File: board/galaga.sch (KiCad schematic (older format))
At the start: 13 parts, among them J1 led_a, J2 speaker_out, J3 led_b, J4 led_c, J5 pwr_in, U1 LD1117S33TR_SOT223, U2 ATmega328P-PU, U3 LM386, U4 BOB-00544

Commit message: added self-power-off hardware to schematic
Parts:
- added Q?: 2N7000, Package_TO_SOT_THT:TO-92_Inline, symbol Transistor_FET:2N7000
- added R?: 10M, symbol Device:R
- added R?: 20K, symbol Device:R
- added R?: 180R, symbol Device:R
- added SW?: SW_Push, symbol Switch:SW_Push
- added U?: LTV-817M, Package_DIP:DIP-4_W10.16mm, symbol Isolator:LTV-817M
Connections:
- net +9V: now also R?.1, SW?.1
- net GND: now also Q?.1 (S), U?.3; no longer J4.2 (Pin_2), J4.3 (Pin_3), R1.2, RV1.1, U1.1 (GND), U2.22 (GND), U2.8 (GND), U3.2 (-), U4.3 (GND)
- net at U2.2 (PD0): no longer J4.1 (Pin_1)
- net PWR_OFF: now reaches U2.9 (XTAL1/PB6)
- net PWR_OFF: now also R?.1
- new net: R1.2, RV1.1
- new net: R?.2, U?.1
- new net: Q?.2 (G), R?.2, U?.4
- new net: R?.1, SW?.2
- new net DGND: J4.1 (Pin_1), J4.2 (Pin_2), J4.3 (Pin_3), Q?.3 (D), R?.2, U1.1 (GND), U2.22 (GND), U2.8 (GND), U3.2 (-), U4.3 (GND), U?.2
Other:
- moved on the sheet: C1, C5, J1, J2, J3, J4, J5, U1, U2, U3, U4

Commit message: started laying out board - doesn't have to be perfect (cuz it's perfboard) and there's some vertical room I'm playing with
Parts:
- removed RV1: 1k, Potentiometer_THT:Potentiometer_Vishay_T7-YA_Single_Vertical, symbol Device:R_POT
- Q1: renamed from Q?; footprint Package_TO_SOT_THT:TO-92_Inline -> Package_TO_SOT_THT:TO-220-3_Vertical
- R2, R3, R4: renamed from R?; footprint (none) -> Resistor_THT:R_Axial_DIN0207_L6.3mm_D2.5mm_P2.54mm_Vertical
- SW1: renamed from SW?; footprint (none) -> TerminalBlock_TE-Connectivity:TerminalBlock_TE_282834-2_1x02_P2.54mm_Horizontal
- U4: footprint custom:bob-00544 -> Connector_PinHeader_2.54mm:PinHeader_1x07_P2.54mm_Vertical
- gave numbers to parts that had none: 1
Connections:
- net sd_cs: now also U2.16 (PB2); no longer U2.6 (PD4)
- net at C1.2: now also R1.2
- net sd_cd: no longer names the net of U2.5 (PD3)
- net sd_cd: no longer U4.1 (CD)
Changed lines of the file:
@@
 EESchema Schematic File Version 4
+LIBS:galaga-cache
 EELAYER 26 0
 EELAYER END
@@
 F 0 "U4" H 8381 3425 50  0000 C CNN
 F 1 "BOB-00544" H 8381 3334 50  0000 C CNN
-F 2 "custom:bob-00544" H 8300 3900 50  0001 C CNN
+F 2 "Connector_PinHeader_2.54mm:PinHeader_1x07_P2.54mm_Vertical" H 8300 3900 50  0001 C CNN
 F 3 "" H 8300 3900 50  0001 C CNN
 	1    8350 2900
@@
 Wire Wire Line
 	7750 2200 6050 2200
-Wire Wire Line
-	7550 3200 8100 3200
 Text GLabel 8050 3000 0    50   Input ~ 0
 DGND
@@
 Wire Wire Line
 	6050 3300 6400 3300
-Wire Wire Line
-	7550 3200 7550 3900
-Wire Wire Line
-	6050 3900 7550 3900
 Text HLabel 8050 2600 0    50   Input ~ 0
 sd_cs
 Wire Wire Line
 	8050 2600 8100 2600
-Text HLabel 6100 4000 2    50   Input ~ 0
+Text HLabel 6100 2100 2    50   Input ~ 0
 sd_cs
-Wire Wire Line
-	6050 4000 6100 4000
 Text Label 7200 2200 0    50   ~ 0
 sd_di
-Text Label 7550 3300 0    50   ~ 0
-sd_cd
 Text Label 7200 2400 0    50   ~ 0
 sd_sck
@@
 	1    0    0    -1
 $EndComp
-$Comp
-L Device:R_POT RV1
-U 1 1 5C58E151
-P 7000 2000
-F 0 "RV1" V 6886 2000 50  0001 C CNN
-F 1 "1k" V 7000 2000 50  0000 C CNN
-F 2 "Potentiometer_THT:Potentiometer_Vishay_T7-YA_Single_Vertical" H 7000 2000 50  0001 C CNN
-F 3 "~" H 7000 2000 50  0001 C CNN
-	1    7000 2000
-	0    -1   -1   0
-$EndComp
 Wire Wire Line
 	6050 2000 6100 2000
@@
 Wire Wire Line
 	8100 1400 8100 2000
-Wire Wire Line
-	8100 2000 7200 2000
-Wire Wire Line
-	7000 1850 7000 1800
-Wire Wire Line
-	7000 1800 7200 1800
-Wire Wire Line
-	7200 1800 7200 2000
-Wire Wire Line
-	7200 2000 7150 2000
 Text Notes 6200 1600 0    50   ~ 0
 With 3.3v max out of the m328, \nthis guarantees a maximum of \n2.62v into the amp. This would \nclip on full strength signals, but \nit allows us to take advantage of \nthe fact that audio is very rarely \nfull strength.
@@
 	8600 1500 8750 1500
 $Comp
-L Isolator:LTV-817M U?
+L Isolator:LTV-817M U5
 U 1 1 5D708174
 P 2450 2150
-F 0 "U?" H 2450 2475 50  0001 C CNN
+F 0 "U5" H 2450 2475 50  0001 C CNN
 F 1 "LTV-817M" H 2450 2384 50  0001 C CNN
 F 2 "Package_DIP:DIP-4_W10.16mm" H 2450 1850 50  0001 C CNN
@@
 $EndComp
 $Comp
-L Transistor_FET:2N7000 Q?
+L Transistor_FET:2N7000 Q1
 U 1 1 5D708462
 P 1450 1950
-F 0 "Q?" H 1655 1996 50  0001 L CNN
+F 0 "Q1" H 1655 1996 50  0001 L CNN
 F 1 "2N7000" H 1655 1905 50  0001 L CNN
-F 2 "Package_TO_SOT_THT:TO-92_Inline" H 1650 1875 50  0001 L CIN
+F 2 "Package_TO_SOT_THT:TO-220-3_Vertical" H 1650 1875 50  0001 L CIN
 F 3 "https://www.fairchildsemi.com/datasheets/2N/2N7000.pdf" H 1450 1950 50  0001 L CNN
 	1    1450 1950
@@
 $EndComp
 $Comp
-L Device:R R?
+L Device:R R2
 U 1 1 5D7084DD
 P 1350 1500
-F 0 "R?" H 1420 1546 50  0000 L CNN
+F 0 "R2" H 1420 1546 50  0000 L CNN
 F 1 "10M" H 1420 1455 50  0000 L CNN
-F 2 "" V 1280 1500 50  0001 C CNN
+F 2 "Resistor_THT:R_Axial_DIN0207_L6.3mm_D2.5mm_P2.54mm_Vertical" V 1280 1500 50  0001 C CNN
 F 3 "~" H 1350 1500 50  0001 C CNN
 	1    1350 1500
@@
 $EndComp
 $Comp
-L Device:R R?
+L Device:R R3
 U 1 1 5D70854B
 P 2750 1650
-F 0 "R?" H 2820 1696 50  0000 L CNN
+F 0 "R3" H 2820 1696 50  0000 L CNN
 F 1 "20K" H 2820 1605 50  0000 L CNN
-F 2 "" V 2680 1650 50  0001 C CNN
+F 2 "Resistor_THT:R_Axial_DIN0207_L6.3mm_D2.5mm_P2.54mm_Vertical" V 2680 1650 50  0001 C CNN
 F 3 "~" H 2750 1650 50  0001 C CNN
 	1    2750 1650
@@
 $EndComp
 $Comp
-L Switch:SW_Push SW?
+L Switch:SW_Push SW1
 U 1 1 5D7085A6
 P 2750 1100
-F 0 "SW?" V 2704 1248 50  0001 L CNN
+F 0 "SW1" V 2704 1248 50  0001 L CNN
 F 1 "SW_Push" V 2795 1248 50  0001 L CNN
-F 2 "" H 2750 1300 50  0001 C CNN
+F 2 "TerminalBlock_TE-Connectivity:TerminalBlock_TE_282834-2_1x02_P2.54mm_Horizontal" H 2750 1300 50  0001 C CNN
 F 3 "" H 2750 1300 50  0001 C CNN
 	1    2750 1100
 	0    1    1    0
 $EndComp
-Connection ~ 7200 2000
 Wire Wire Line
 	6050 2400 7650 2400
@@
 Wire Wire Line
 	8350 1250 8350 1600
-Wire Wire Line
-	6400 2000 6850 2000
 Text GLabel 6400 3400 0    50   Input ~ 0
 DGND
@@
 	1200 2250 1350 2250
 $Comp
-L Device:R R?
+L Device:R R4
 U 1 1 5D77529A
 P 2950 2050
-F 0 "R?" V 2743 2050 50  0000 C CNN
+F 0 "R4" V 2743 2050 50  0000 C CNN
 F 1 "180R" V 2834 2050 50  0000 C CNN
-F 2 "" V 2880 2050 50  0001 C CNN
+F 2 "Resistor_THT:R_Axial_DIN0207_L6.3mm_D2.5mm_P2.54mm_Vertical" V 2880 2050 50  0001 C CNN
 F 3 "~" H 2950 2050 50  0001 C CNN
 	1    2950 2050
@@
 Wire Wire Line
 	2750 1300 2750 1500
+Wire Wire Line
+	6400 2000 8100 2000
+Wire Wire Line
+	6100 2100 6050 2100
 $EndSCHEMATC

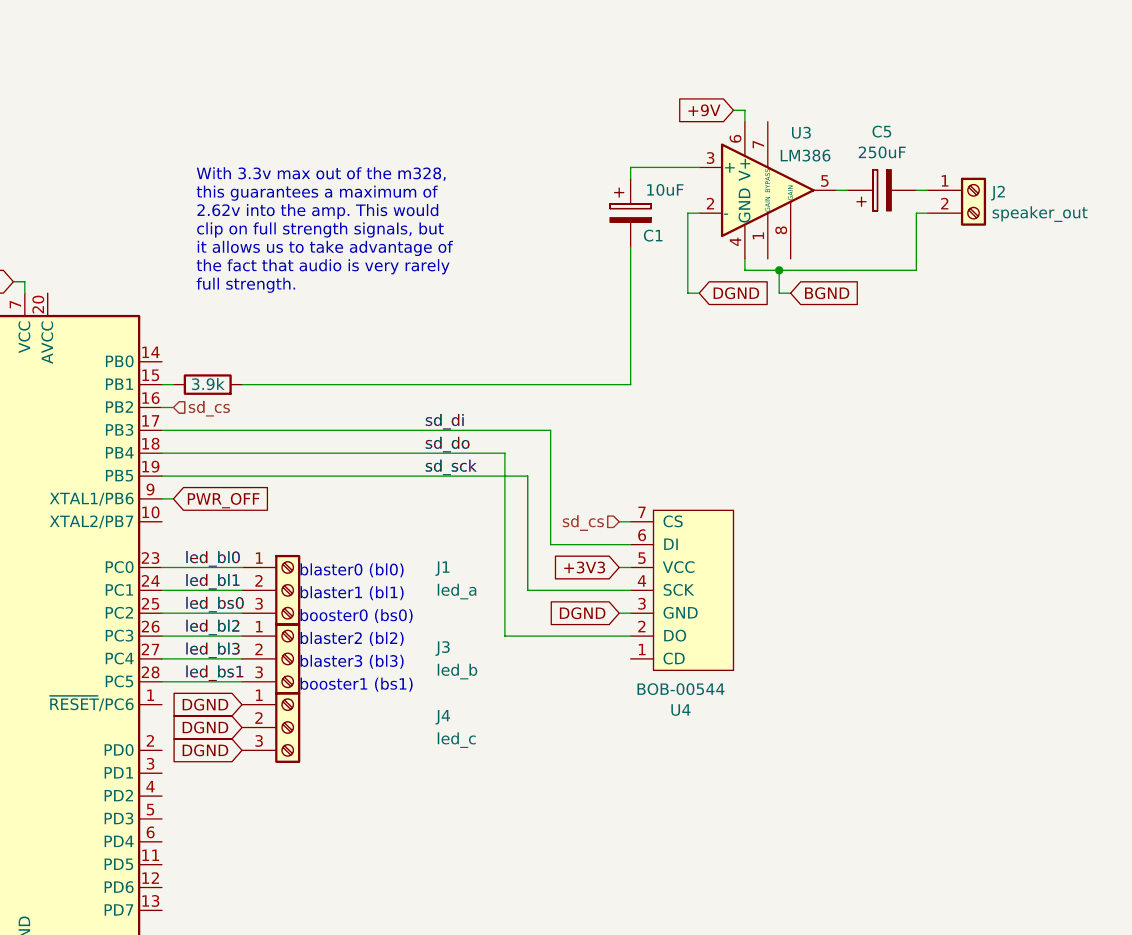
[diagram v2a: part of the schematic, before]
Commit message: changed SD CS pin to PORTB7 for better board layout
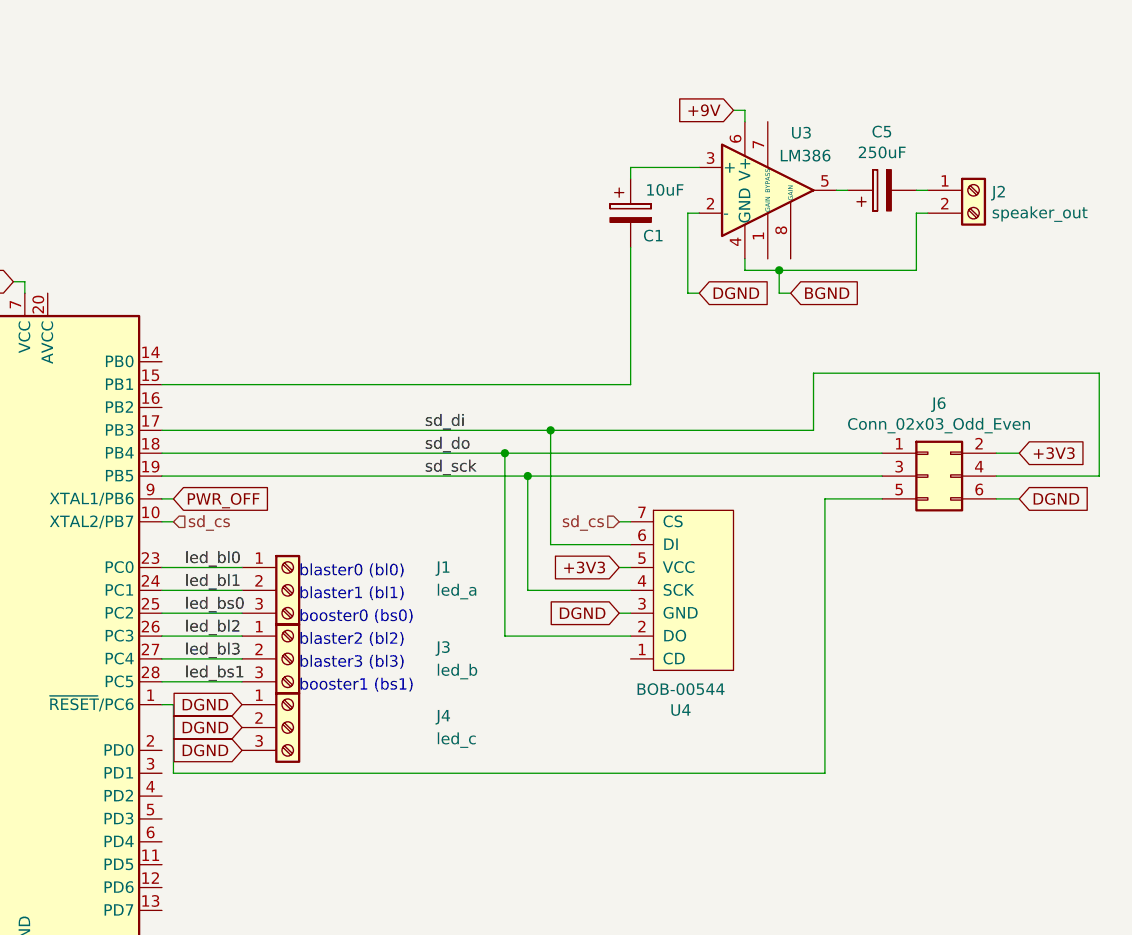
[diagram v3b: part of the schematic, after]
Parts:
- removed R1: 3.9k, Resistor_THT:R_Axial_DIN0207_L6.3mm_D2.5mm_P2.54mm_Vertical, symbol Device:R
- added J6: Conn_02x03_Odd_Even, Connector_PinHeader_2.54mm:PinHeader_2x03_P2.54mm_Vertical, symbol Connector_Generic:Conn_02x03_Odd_Even
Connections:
- net +3V3: now also J6.2 (Pin_2)
- net DGND: now also J6.6 (Pin_6)
- net sd_cs: now also U2.10 (XTAL2/PB7); no longer U2.16 (PB2)
- net sd_di: now also J6.4 (Pin_4)
- net sd_do: now also J6.1 (Pin_1)
- net sd_sck: now also J6.3 (Pin_3)
- net at U2.1 (~RESET~/PC6): now also J6.5 (Pin_5)
- net at U2.15 (PB1): now also C1.2
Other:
- note removed: "With 3.3v max out of the m328, \nthis guarantees a maximum of \n2.62v into the amp. This would \nclip on full strength signals, but \nit allows us to take advantage of \nthe fact that audio is very rarely \nfull strength."
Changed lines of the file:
@@
-$EndComp
-$Comp
-L Device:R R1
-U 1 1 5BBECF45
-P 6250 2000
-F 0 "R1" V 6600 2000 50  0001 R CNN
-F 1 "3.9k" V 6250 2000 50  0000 C CNN
-F 2 "Resistor_THT:R_Axial_DIN0207_L6.3mm_D2.5mm_P2.54mm_Vertical" V 6180 2000 50  0001 C CNN
-F 3 "~" H 6250 2000 50  0001 C CNN
-	1    6250 2000
-	0    -1   -1   0
 $EndComp
 $Comp
@@
 Wire Wire Line
 	8050 2600 8100 2600
-Text HLabel 6100 2100 2    50   Input ~ 0
+Text HLabel 6100 2600 2    50   Input ~ 0
 sd_cs
 Text Label 7200 2200 0    50   ~ 0
@@
 $EndComp
 Wire Wire Line
-	6050 2000 6100 2000
-Wire Wire Line
 	8400 1050 8100 1050
 Wire Wire Line
@@
 Wire Wire Line
 	8100 1400 8100 2000
-Text Notes 6200 1600 0    50   ~ 0
-With 3.3v max out of the m328, \nthis guarantees a maximum of \n2.62v into the amp. This would \nclip on full strength signals, but \nit allows us to take advantage of \nthe fact that audio is very rarely \nfull strength.
 Wire Wire Line
 	9000 1150 9050 1150
@@
 Wire Wire Line
 	2750 1300 2750 1500
-Wire Wire Line
-	6400 2000 8100 2000
-Wire Wire Line
-	6100 2100 6050 2100
+$Comp
+L Connector_Generic:Conn_02x03_Odd_Even J6
+U 1 1 5D757B8F
+P 9400 2400
+F 0 "J6" H 9450 2717 50  0000 C CNN
+F 1 "Conn_02x03_Odd_Even" H 9450 2626 50  0000 C CNN
+F 2 "Connector_PinHeader_2.54mm:PinHeader_2x03_P2.54mm_Vertical" H 9400 2400 50  0001 C CNN
+F 3 "~" H 9400 2400 50  0001 C CNN
+	1    9400 2400
+	1    0    0    -1
+$EndComp
+Connection ~ 7550 2300
+Connection ~ 7650 2400
+Wire Wire Line
+	6050 3400 6100 3400
+Wire Wire Line
+	6100 3400 6100 3700
+Wire Wire Line
+	6100 3700 8950 3700
+Wire Wire Line
+	8950 3700 8950 2500
+Wire Wire Line
+	8950 2500 9200 2500
+Text GLabel 9800 2300 2    50   Input ~ 0
++3V3
+Wire Wire Line
+	9800 2300 9700 2300
+Text GLabel 9800 2500 2    50   Input ~ 0
+DGND
+Wire Wire Line
+	9800 2500 9700 2500
+Wire Wire Line
+	7650 2400 9200 2400
+Wire Wire Line
+	7550 2300 9200 2300
+Wire Wire Line
+	7750 2200 8900 2200
+Wire Wire Line
+	8900 2200 8900 1950
+Wire Wire Line
+	8900 1950 10150 1950
+Wire Wire Line
+	10150 1950 10150 2400
+Wire Wire Line
+	10150 2400 9700 2400
+Connection ~ 7750 2200
+Wire Wire Line
+	6050 2000 8100 2000
+Wire Wire Line
+	6100 2600 6050 2600
 $EndSCHEMATC

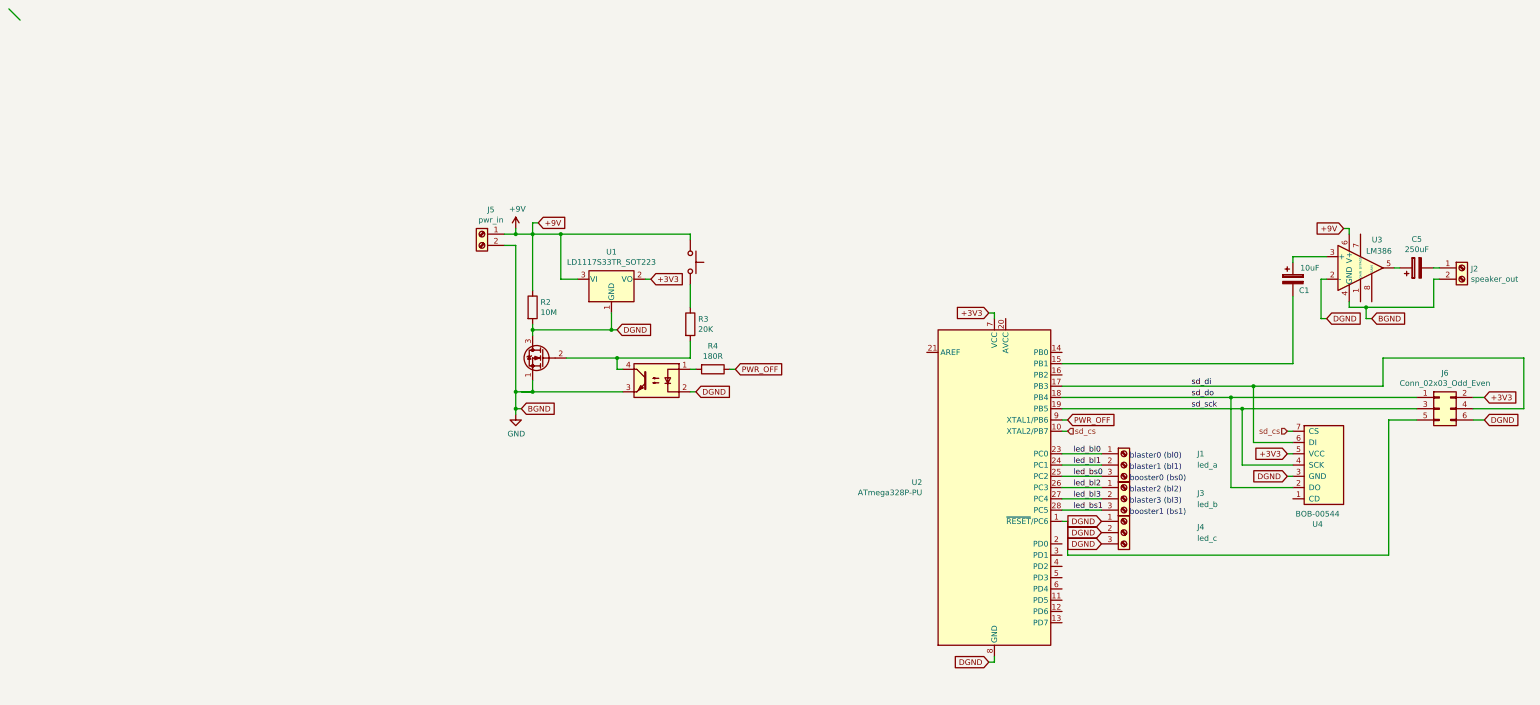
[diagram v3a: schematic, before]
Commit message: revamped power and amp circuits, going back to breadboard testing before circuit construction
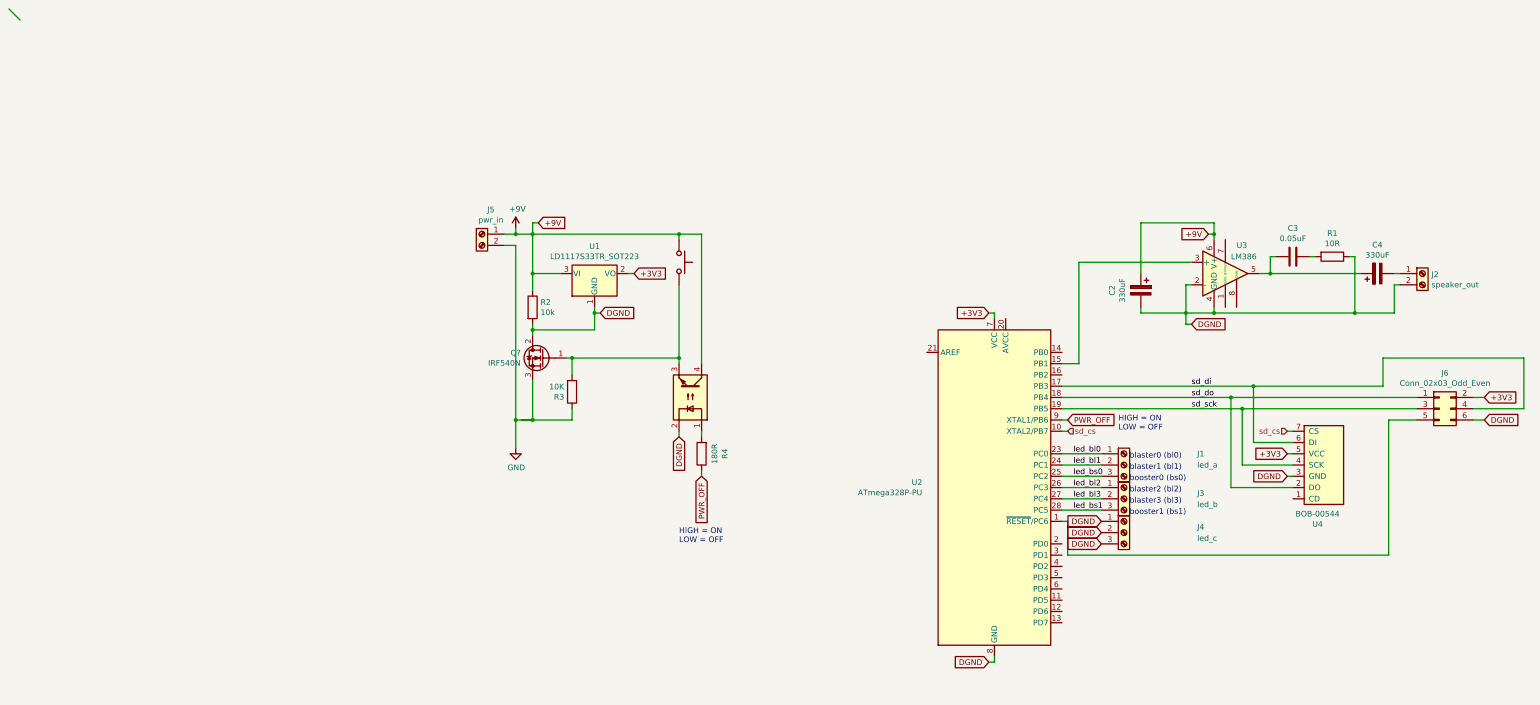
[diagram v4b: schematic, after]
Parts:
- removed C1: 10uF, Capacitor_THT:CP_Axial_L10.0mm_D6.0mm_P15.00mm_Horizontal, symbol Device:CP
- removed C5: 250uF, Capacitor_THT:CP_Axial_L20.0mm_D10.0mm_P26.00mm_Horizontal, symbol Device:CP
- removed Q1: 2N7000, Package_TO_SOT_THT:TO-220-3_Vertical, symbol Transistor_FET:2N7000
- added C2, C4: 330uF, Capacitor_THT:CP_Radial_D10.0mm_P5.00mm, symbol Device:CP
- added C3: 0.05uF, Capacitor_THT:C_Disc_D12.0mm_W4.4mm_P7.75mm, symbol Device:C
- added Q?: IRF540N, Package_TO_SOT_THT:TO-220-3_Vertical, symbol Transistor_FET:IRF540N
- added R1: 10R, Resistor_THT:R_Axial_DIN0207_L6.3mm_D2.5mm_P2.54mm_Vertical, symbol Device:R
- R2: value 10M -> 10k
- R3: value 20K -> 10K
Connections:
- net +9V: now also U5.4, C2.1
- net DGND: now also J2.2 (Pin_2), U3.4 (GND), C2.2, Q?.2 (D), R1.1
- net GND: now also R3.1, Q?.3 (S); no longer J2.2 (Pin_2), U3.4 (GND), U5.3
- net at U3.3 (+): now also U2.15 (PB1)
- net at U3.5: now also C3.2, C4.1
- net at J2.1 (Pin_1): now also C4.2
- net at R3.2: now also SW1.2, U5.3, Q?.1 (G); no longer U5.4
- new net: C3.1, R1.2
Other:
- note added: "HIGH = ON\nLOW = OFF"
- moved on the sheet: J2, R3, R4, U1, U3

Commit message: finished the board, worked first shot!
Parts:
- gave numbers to parts that had none: 1
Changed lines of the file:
@@
 	6200 1100 6200 2000
 $Comp
-L Transistor_FET:IRF540N Q?
+L Transistor_FET:IRF540N Q1
 U 1 1 5E19A72B
 P 1450 1950
-F 0 "Q?" H 1656 1996 50  0000 L CNN
+F 0 "Q1" H 1656 1996 50  0000 L CNN
 F 1 "IRF540N" H 1656 1905 50  0000 L CNN
 F 2 "Package_TO_SOT_THT:TO-220-3_Vertical" H 1700 1875 50  0001 L CIN

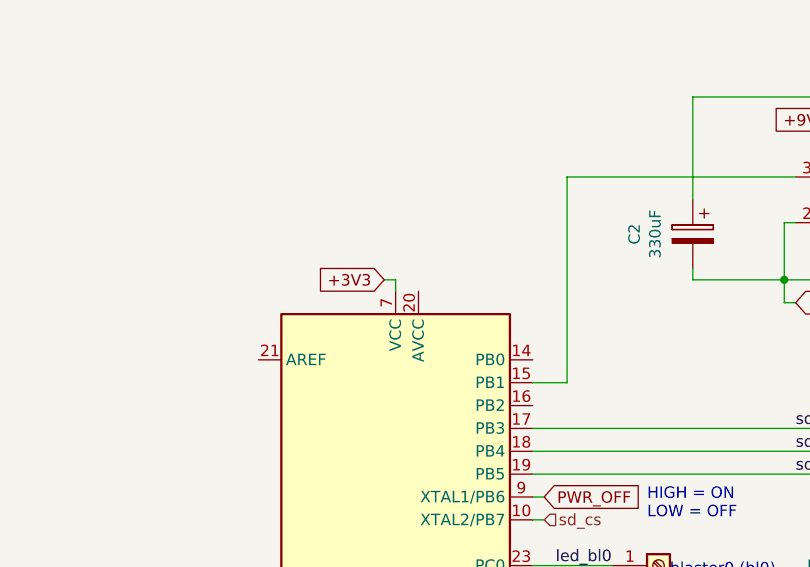
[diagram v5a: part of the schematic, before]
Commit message: fixed poweroff - one line!!!!! -_-
Random is still having trouble - it seems like it's sorta getting kinda
random stuff, but it's a little too consistent for my taste. I'll have
to do some testing.
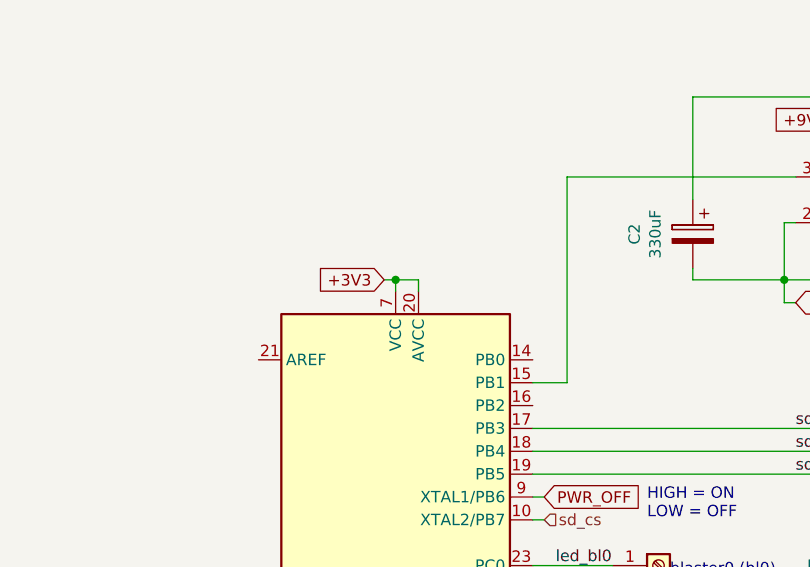
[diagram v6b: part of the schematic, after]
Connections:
- net +3V3: now also U2.20 (AVCC)
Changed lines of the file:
@@
 Wire Wire Line
 	1200 2500 1200 2750
+Wire Wire Line
+	5450 1550 5550 1550
+Wire Wire Line
+	5550 1550 5550 1600
+Connection ~ 5450 1550
 $EndSCHEMATC
